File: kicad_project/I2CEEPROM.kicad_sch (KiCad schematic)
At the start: 3 parts, among them U15 24FC64-I/SN

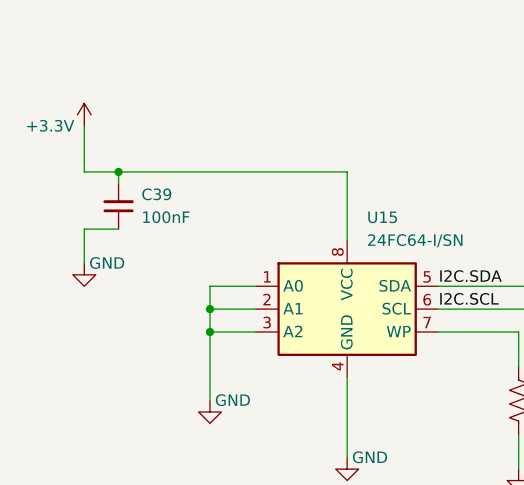
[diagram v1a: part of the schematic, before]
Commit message: Finish schematic and placement for all remaining RP2354 power passives
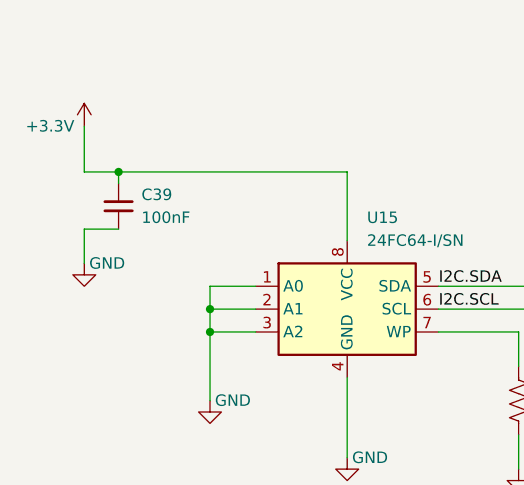
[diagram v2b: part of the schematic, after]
